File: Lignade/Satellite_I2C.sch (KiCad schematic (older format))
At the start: 1 part, among them M1 MODULE_I2C

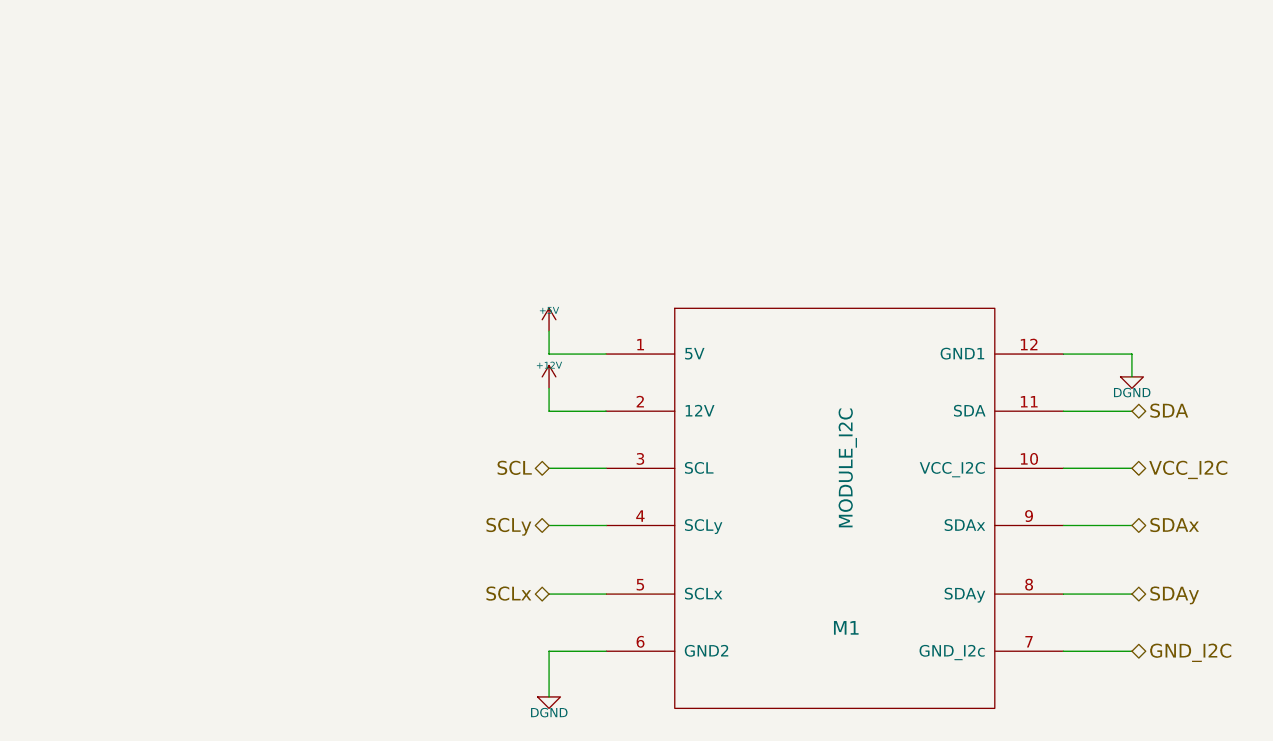
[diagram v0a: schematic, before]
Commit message: Remplacement Bus I2C grande distance par Arduino Mini + RS485. Reste : ADC à porter vers module capteur. Renommer nouveaux composants. Vérifier Cablage.
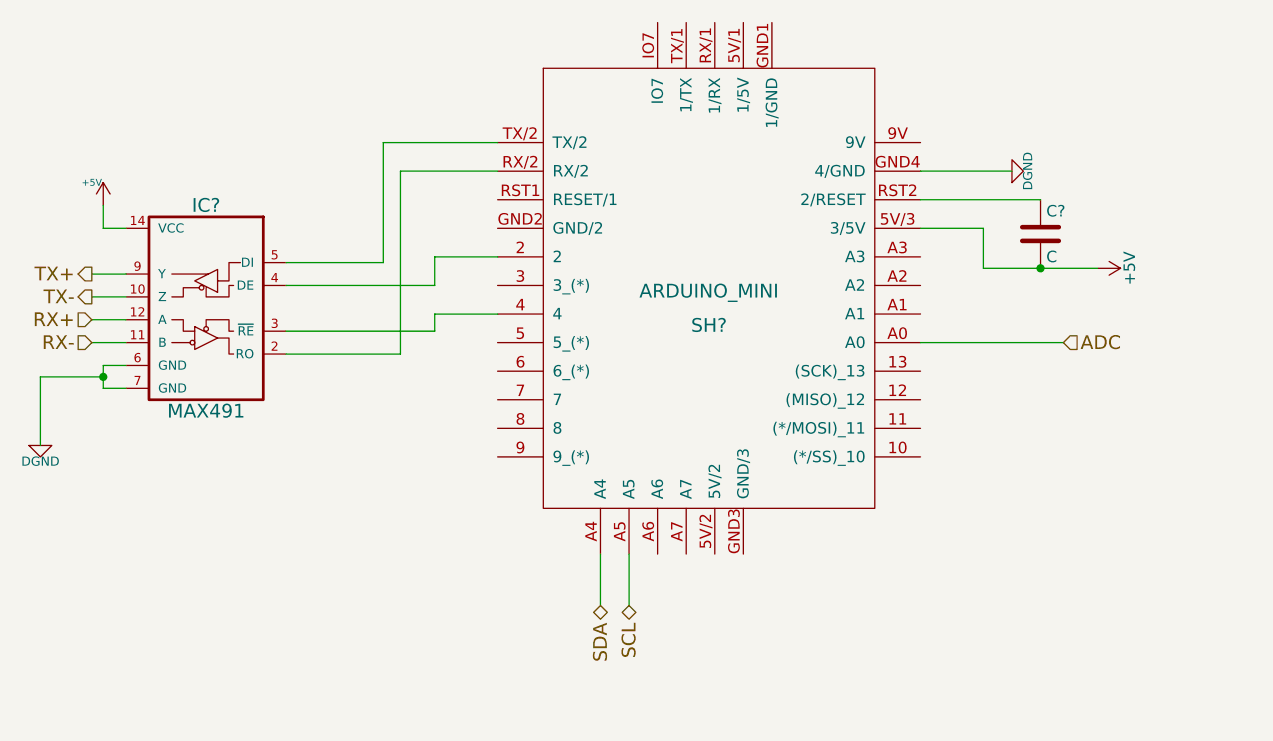
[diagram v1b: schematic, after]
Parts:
- removed M1: MODULE_I2C, symbol MODULE_I2C
- added C?: C, symbol C
- added IC?: MAX491, symbol MAX491
- added SH?: ARDUINO_MINI, symbol ARDUINO_MINI
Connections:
- net +5V: now also C?.2, IC?.14 (VCC), SH?.5V/3 (3/5V)
- net DGND: now also IC?.6 (GND), IC?.7 (GND), SH?.GND4 (4/GND)
- net SCL: now also SH?.A5
- net SDA: now also SH?.A4
- new net: IC?.2 (RO), SH?.RX/2
- new net: IC?.3 (~RE), SH?.4
- new net: IC?.4 (DE), SH?.2
- new net: IC?.5 (DI), SH?.TX/2
- new net: C?.1, SH?.RST2 (2/RESET)
- new net ADC: SH?.A0
- new net RX+: IC?.12 (A)
- new net RX-: IC?.11 (B)
- new net TX+: IC?.9 (Y)
- new net TX-: IC?.10 (Z)
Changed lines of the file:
@@
-EESchema Schematic File Version 2  date mar. 10 mai 2011 21:09:00 ICT
+EESchema Schematic File Version 2
+LIBS:Satellite-rescue
 LIBS:power
 LIBS:device
@@
 LIBS:memory
 LIBS:xilinx
-LIBS:special
 LIBS:microcontrollers
 LIBS:dsp
@@
 LIBS:Lignade
 LIBS:i2c
+LIBS:ok-ic-com
+LIBS:shield_arduino
 LIBS:Satellite-cache
-EELAYER 24  0
+EELAYER 25 0
 EELAYER END
-$Descr A4 11700 8267
-Sheet 5 6
+$Descr A4 11693 8268
+encoding utf-8
+Sheet 6 6
 Title ""
 Date "10 may 2011"
@@
 Comment4 ""
 $EndDescr
-Wire Wire Line
-	4300 2100 4300 2200
-Wire Wire Line
-	4300 2200 4550 2200
-Wire Wire Line
-	4300 2700 4550 2700
-Wire Wire Line
-	4300 3250 4550 3250
-Wire Wire Line
-	4300 3700 4300 3500
-Wire Wire Line
-	6850 3250 6550 3250
-Wire Wire Line
-	6850 2700 6550 2700
-Wire Wire Line
-	6850 2450 6550 2450
-Wire Wire Line
-	6850 2300 6850 2200
-Wire Wire Line
-	6850 2200 6550 2200
-Wire Wire Line
-	6550 2950 6850 2950
-Wire Wire Line
-	6550 3500 6850 3500
-Wire Wire Line
-	4300 3500 4550 3500
-Wire Wire Line
-	4550 2950 4300 2950
-Wire Wire Line
-	4550 2450 4300 2450
-Wire Wire Line
-	4300 2450 4300 2350
-$Comp
-L DGND #PWR22
-U 1 1 4DAA6FB7
-P 6850 2300
-F 0 "#PWR22" H 6850 2300 40  0001 C CNN
-F 1 "DGND" H 6850 2230 40  0000 C CNN
-	1    6850 2300
-	1    0    0    -1
-$EndComp
 $Comp
 L DGND #PWR24
 U 1 1 4DAA6FB4
-P 4300 3700
-F 0 "#PWR24" H 4300 3700 40  0001 C CNN
-F 1 "DGND" H 4300 3630 40  0000 C CNN
-	1    4300 3700
-	1    0    0    -1
-$EndComp
-$Comp
-L MODULE_I2C M1
-U 1 1 4DAA6F43
-P 5750 3050
-F 0 "M1" H 5600 2700 60  0000 C CNN
-F 1 "MODULE_I2C" V 5600 3400 60  0000 C CNN
-	1    5750 3050
-	1    0    0    -1
-$EndComp
-Text HLabel 4300 2700 0    60   BiDi ~ 0
-SCL
-Text HLabel 6850 2450 2    60   BiDi ~ 0
-SDA
-Text HLabel 4300 2950 0    60   BiDi ~ 0
-SCLy
-Text HLabel 6850 3250 2    60   BiDi ~ 0
-SDAy
-$Comp
-L +12V #PWR014
-U 1 1 4D70E293
-P 4300 2350
-F 0 "#PWR014" H 4300 2300 20  0001 C CNN
-F 1 "+12V" H 4300 2450 30  0000 C CNN
-	1    4300 2350
-	-1   0    0    -1
+P 6325 1400
+F 0 "#PWR24" H 6325 1400 40  0001 C CNN
+F 1 "DGND" H 6325 1330 40  0000 C CNN
+F 2 "" H 6325 1400 60  0001 C CNN
+F 3 "" H 6325 1400 60  0001 C CNN
+	1    6325 1400
+	0    -1   -1   0
 $EndComp
 $Comp
 L +5V #PWR015
 U 1 1 4D6DB7B6
-P 4300 2100
-F 0 "#PWR015" H 4300 2190 20  0001 C CNN
-F 1 "+5V" H 4300 2190 30  0000 C CNN
-	1    4300 2100
+P 2350 1550
+F 0 "#PWR015" H 2350 1640 20  0001 C CNN
+F 1 "+5V" H 2400 1650 30  0000 C CNN
+F 2 "" H 2350 1550 60  0001 C CNN
+F 3 "" H 2350 1550 60  0001 C CNN
+	1    2350 1550
 	-1   0    0    -1
 $EndComp
-Text HLabel 6850 3500 2    60   BiDi ~ 0
-GND_I2C
-Text HLabel 4300 3250 0    60   BiDi ~ 0
-SCLx
-Text HLabel 6850 2700 2    60   BiDi ~ 0
-VCC_I2C
-Text HLabel 6850 2950 2    60   BiDi ~ 0
-SDAx
+Text HLabel 4525 3300 3    60   BiDi ~ 0
+SDA
+Text HLabel 4650 3300 3    60   BiDi ~ 0
+SCL
+Text HLabel 2300 1850 0    60   Output ~ 0
+TX+
+Text HLabel 2300 1950 0    60   Output ~ 0
+TX-
+Text HLabel 2300 2050 0    60   Input ~ 0
+RX+
+Text HLabel 2300 2150 0    60   Input ~ 0
+RX-
+$Comp
+L MAX491 IC?
+U 1 1 556E69A4
+P 2800 2000
+F 0 "IC?" H 2800 2450 60  0000 C CNN
+F 1 "MAX491" H 2800 1550 60  0000 C CNN
+F 2 "" H 2800 2000 60  0000 C CNN
+F 3 "" H 2800 2000 60  0000 C CNN
+	1    2800 2000
+	-1   0    0    -1
+$EndComp
+$Comp
+L ARDUINO_MINI SH?
+U 1 1 556E6B70
+P 5000 1950
+F 0 "SH?" H 5000 1825 60  0000 C CNN
+F 1 "ARDUINO_MINI" H 5000 1975 60  0000 C CNN
+F 2 "" H 4825 3625 60  0000 C CNN
+F 3 "" H 4825 3625 60  0000 C CNN
+	1    5000 1950
+	1    0    0    -1
+$EndComp
+Wire Wire Line
+	2300 1850 2450 1850
+Wire Wire Line
+	2450 1950 2300 1950
+Wire Wire Line
+	2300 2050 2450 2050
+Wire Wire Line
+	2300 2150 2450 2150
+Wire Wire Line
+	2450 2250 2350 2250
+Wire Wire Line
+	2350 2250 2350 2350
+Wire Wire Line
+	2350 2350 2450 2350
+Wire Wire Line
+	5925 1400 6325 1400
+Wire Wire Line
+	2075 2300 2350 2300
+Connection ~ 2350 2300
+Wire Wire Line
+	2350 1550 2350 1650
+Wire Wire Line
+	2350 1650 2450 1650
+Wire Wire Line
+	3150 1800 3575 1800
+Wire Wire Line
+	3575 1800 3575 1275
+Wire Wire Line
+	3575 1275 4075 1275
+Wire Wire Line
+	3150 2200 3650 2200
+Wire Wire Line
+	3650 2200 3650 1400
+Wire Wire Line
+	3650 1400 4075 1400
+Wire Wire Line
+	4075 1775 3800 1775
+Wire Wire Line
+	3800 1775 3800 1900
+Wire Wire Line
+	3800 1900 3150 1900
+Wire Wire Line
+	4075 2025 3800 2025
+Wire Wire Line
+	3800 2025 3800 2100
+Wire Wire Line
+	3800 2100 3150 2100
+Wire Wire Line
+	4650 3300 4650 3075
+Wire Wire Line
+	4525 3300 4525 3075
+$Comp
+L C C?
+U 1 1 556E6DAD
+P 6450 1675
+F 0 "C?" H 6475 1775 50  0000 L CNN
+F 1 "C" H 6475 1575 50  0000 L CNN
+F 2 "" H 6488 1525 30  0000 C CNN
+F 3 "" H 6450 1675 60  0000 C CNN
+	1    6450 1675
+	1    0    0    -1
+$EndComp
+Wire Wire Line
+	6450 1525 5925 1525
+Wire Wire Line
+	5925 1650 6200 1650
+Wire Wire Line
+	6200 1650 6200 1825
+Wire Wire Line
+	6200 1825 6700 1825
+$Comp
+L +5V #PWR?
+U 1 1 556E6E42
+P 6700 1825
+F 0 "#PWR?" H 6700 1675 50  0001 C CNN
+F 1 "+5V" H 6700 1965 50  0000 C CNN
+F 2 "" H 6700 1825 60  0000 C CNN
+F 3 "" H 6700 1825 60  0000 C CNN
+	1    6700 1825
+	0    1    1    0
+$EndComp
+$Comp
+L DGND #PWR?
+U 1 1 556E6F98
+P 2075 2600
+F 0 "#PWR?" H 2075 2600 40  0001 C CNN
+F 1 "DGND" H 2075 2530 40  0000 C CNN
+F 2 "" H 2075 2600 60  0001 C CNN
+F 3 "" H 2075 2600 60  0001 C CNN
+	1    2075 2600
+	1    0    0    -1
+$EndComp
+Wire Wire Line
+	2075 2600 2075 2300
+Connection ~ 6450 1825
+Text HLabel 6550 2150 2    60   Input ~ 0
+ADC
+Wire Wire Line
+	6550 2150 5925 2150
 $EndSCHEMATC
